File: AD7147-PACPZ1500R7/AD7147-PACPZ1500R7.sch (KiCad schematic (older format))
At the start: 7 parts, among them J1 Conn_01x07_Male, J2 Conn_01x07_Male, U1 AD7147PACPZ1500R7, U1 TC1264

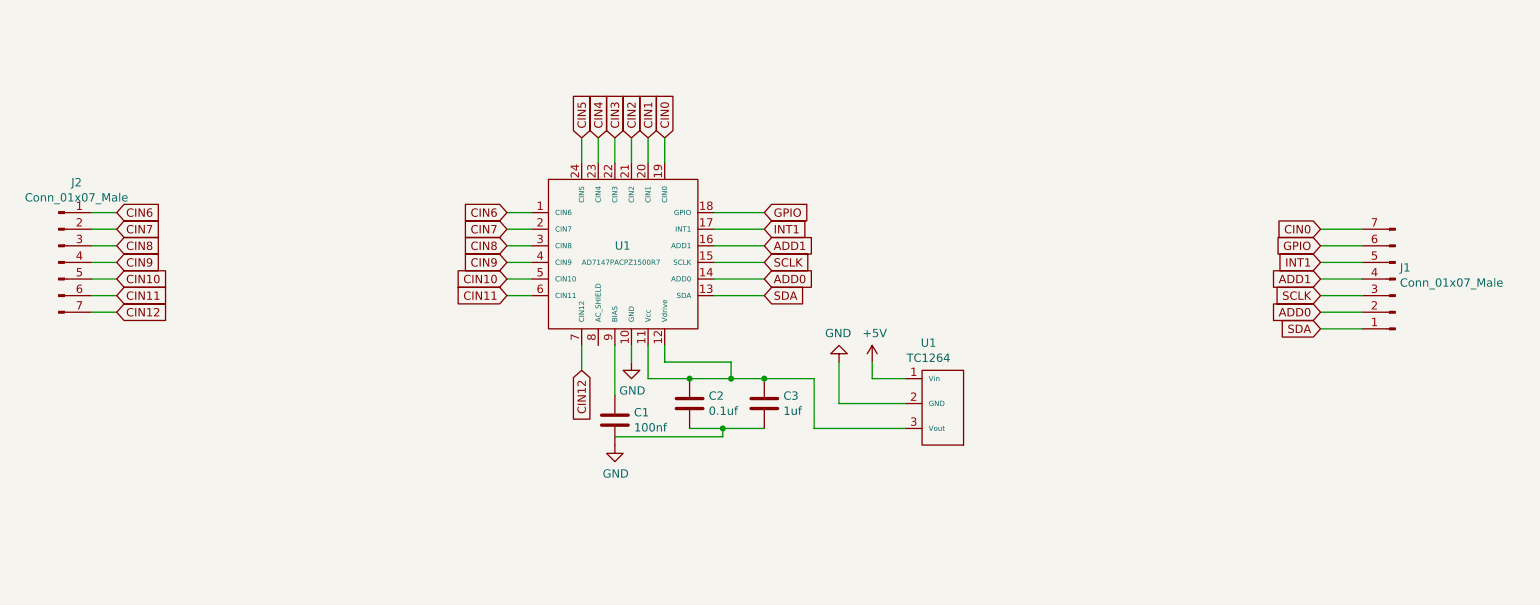
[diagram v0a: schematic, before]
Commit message: Complete AD7147 breakout and create Cap Touch pad
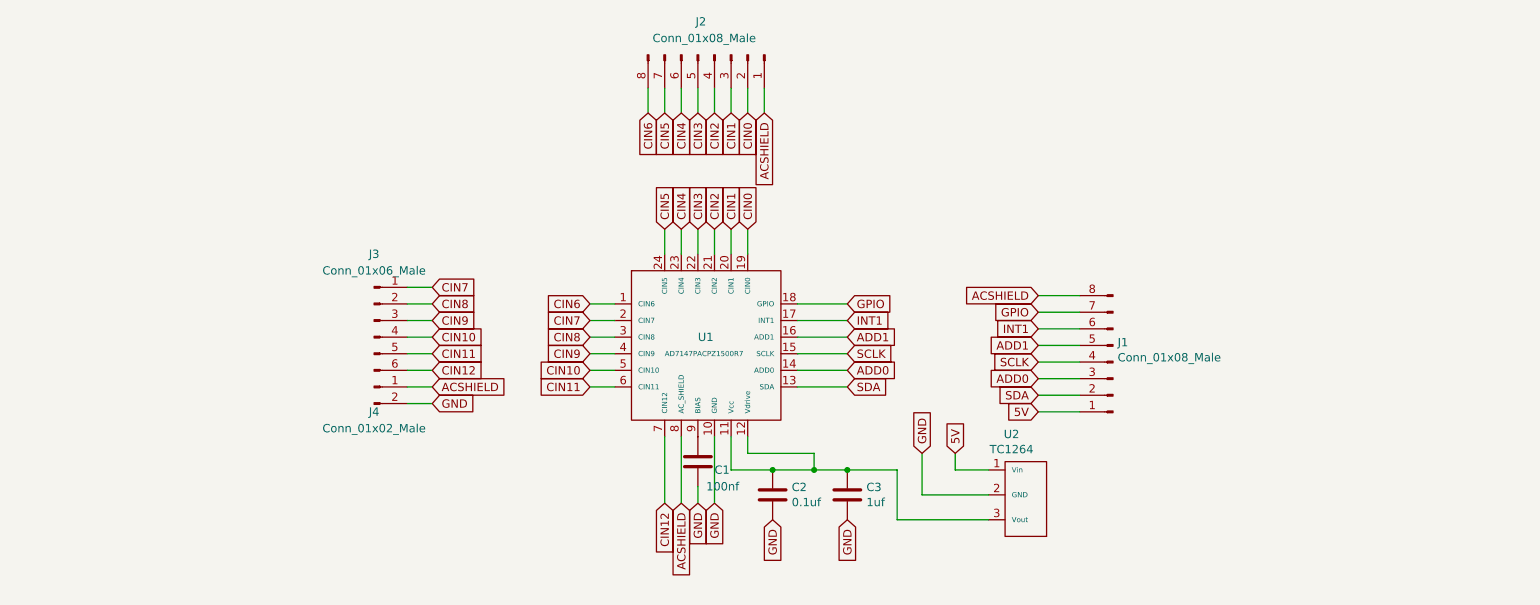
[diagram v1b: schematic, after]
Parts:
- removed J1, J2: Conn_01x07_Male, symbol Connector:Conn_01x07_Male
- added J1, J2: Conn_01x08_Male, Connector_PinHeader_2.54mm:PinHeader_1x08_P2.54mm_Vertical, symbol Connector:Conn_01x08_Male
- added J3: Conn_01x06_Male, Connector_PinHeader_2.54mm:PinHeader_1x06_P2.54mm_Vertical, symbol Connector:Conn_01x06_Male
- added J4: Conn_01x02_Male, Connector_PinHeader_2.54mm:PinHeader_1x02_P2.54mm_Vertical, symbol Connector:Conn_01x02_Male
- U1: footprint (none) -> AD7147-PACPZ1500R7:AD7147-PACPZ1500R7
- renumbered U1 to U2
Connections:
- net ADD0: now also J1.3 (Pin_3)
- net ADD1: now also J1.5 (Pin_5)
- net CIN0: now also J2.2 (Pin_2)
- net CIN1: now also J2.3 (Pin_3)
- net CIN10: now also J3.4 (Pin_4)
- net CIN11: now also J3.5 (Pin_5)
- net CIN12: now also J3.6 (Pin_6)
- net CIN2: now also J2.4 (Pin_4)
- net CIN3: now also J2.5 (Pin_5)
- net CIN4: now also J2.6 (Pin_6)
- net CIN5: now also J2.7 (Pin_7)
- net CIN6: now also J2.8 (Pin_8)
- net CIN7: now also J3.1 (Pin_1)
- net CIN8: now also J3.2 (Pin_2)
- net CIN9: now also J3.3 (Pin_3)
- net GND: now also C2.2, C3.2, J4.2 (Pin_2)
- net GPIO: now also J1.7 (Pin_7)
- net INT1: now also J1.6 (Pin_6)
- net SCLK: now also J1.4 (Pin_4)
- net SDA: now also J1.2 (Pin_2)
- net ACSHIELD: now reaches U1.8 (AC_SHIELD)
- net ACSHIELD: now also J1.8 (Pin_8), J2.1 (Pin_1), J4.1 (Pin_1)
- net +5V renamed 5V
- net 5V: now also J1.1 (Pin_1)
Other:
- moved on the sheet: C1, C2, C3, U1, U2
